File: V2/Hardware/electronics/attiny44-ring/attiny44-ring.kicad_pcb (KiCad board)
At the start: 2 copper layers, 35 x 70 mm, 20 parts, among them J1 CHAIN_IN, J2 CHAIN_OUT, J3 28BYJ-48, J4 HOME_SENSOR, J5 AVR_ISP_2X3, J6 5V_INJECT, U1 ATtiny44A-SS, U2 ULN2003A

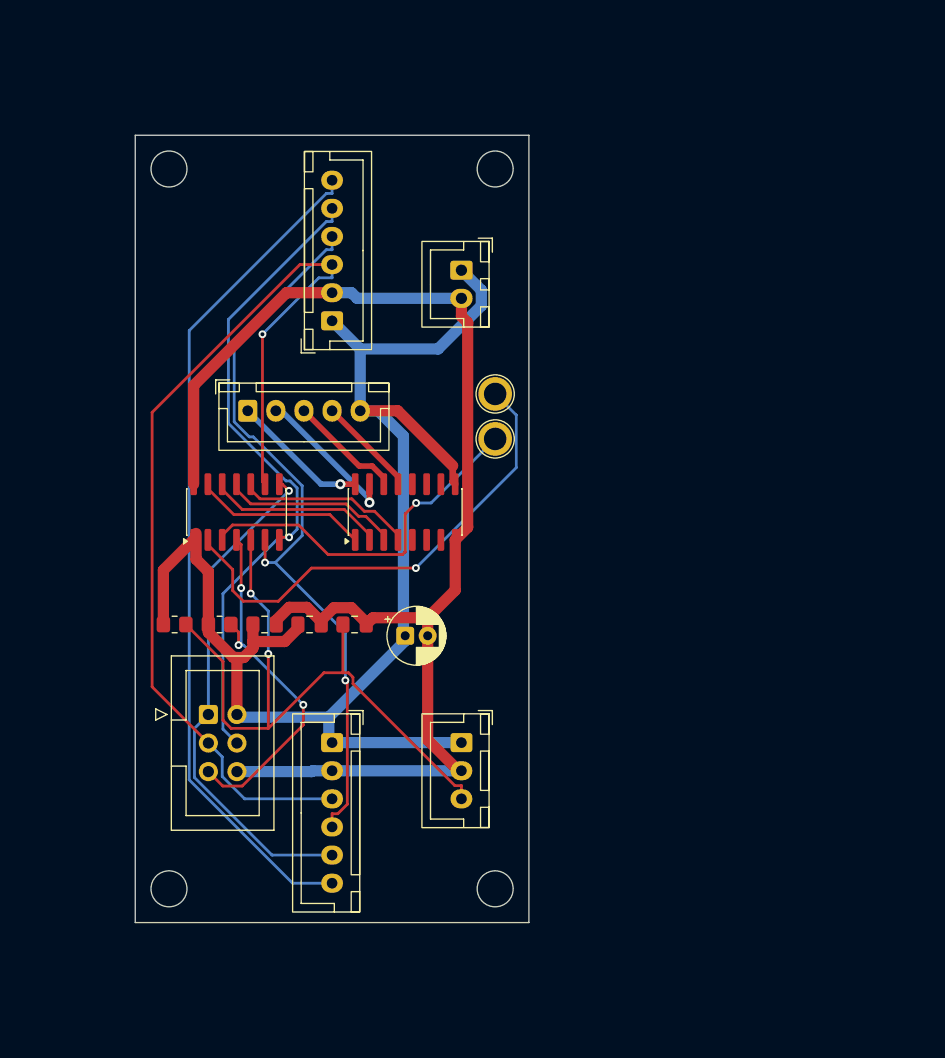
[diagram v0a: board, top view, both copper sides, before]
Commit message: Redesign ATtiny44 ring board for milling
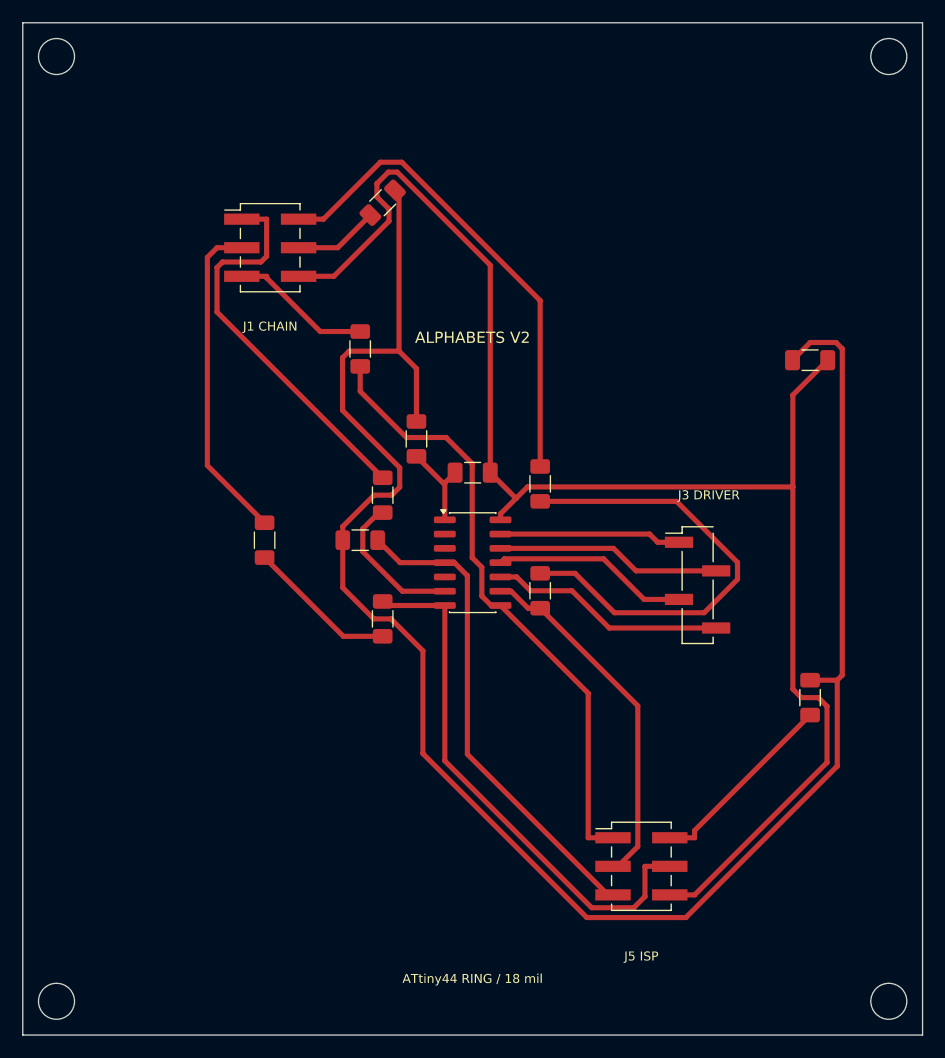
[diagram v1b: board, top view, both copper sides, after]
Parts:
- removed C3: 10n HOME filter, Capacitor_SMD:C_0805_2012Metric_Pad1.18x1.45mm_HandSolder
- removed C4: 47u 10V, Capacitor_THT:CP_Radial_D5.0mm_P2.00mm
- removed J2: CHAIN_OUT, Connector_JST:JST_XH_B6B-XH-A_1x06_P2.50mm_Vertical
- removed J4: HOME_SENSOR, Connector_JST:JST_XH_B3B-XH-A_1x03_P2.50mm_Vertical
- removed J6: 5V_INJECT, Connector_JST:JST_XH_B2B-XH-A_1x02_P2.50mm_Vertical
- removed R1: 10k HOME pull-up, Resistor_SMD:R_0805_2012Metric_Pad1.20x1.40mm_HandSolder
- removed TP1: PB0, TestPoint:TestPoint_Plated_Hole_D2.0mm
- removed TP2: PB1, TestPoint:TestPoint_Plated_Hole_D2.0mm
- removed U2: ULN2003A, Package_SO:SOIC-16_3.9x9.9mm_P1.27mm
- added JP16: 0R CLOCK MCU bridge 1206, Resistor_SMD:R_1206_3216Metric_Pad1.30x1.75mm_HandSolder, F.Cu at (136.0, 140.5)
- added JP17: 0R DATA chain bridge 1206, Resistor_SMD:R_1206_3216Metric_Pad1.30x1.75mm_HandSolder, F.Cu at (111.5, 136.0)
- added JP18: 0R MCU power bridge 1206, Resistor_SMD:R_1206_3216Metric_Pad1.30x1.75mm_HandSolder, F.Cu at (125.0, 127.0)
- added JP19: 0R CHAIN power bridge 1206, Resistor_SMD:R_1206_3216Metric_Pad1.30x1.75mm_HandSolder, F.Cu at (122.0, 106.0)
- added JP20: 0R ISP VCC bridge 1206, Resistor_SMD:R_1206_3216Metric_Pad1.30x1.75mm_HandSolder, F.Cu at (160.0, 150.0)
- added JP5: 0R CLOCK input jumper 1206, Resistor_SMD:R_1206_3216Metric_Pad1.30x1.75mm_HandSolder, F.Cu at (136.0, 131.0)
- added JP6: 0R LATCH input jumper 1206, Resistor_SMD:R_1206_3216Metric_Pad1.30x1.75mm_HandSolder, F.Cu at (122.0, 132.0)
- added JP7: 0R DATA input jumper 1206, Resistor_SMD:R_1206_3216Metric_Pad1.30x1.75mm_HandSolder, F.Cu at (122.0, 143.0)
- added JP8: 0R CHAIN DATA_OUT jumper 1206, Resistor_SMD:R_1206_3216Metric_Pad1.30x1.75mm_HandSolder, F.Cu at (120.0, 119.0)
- C1: value 100n MCU -> 100n MCU 1206; footprint Capacitor_SMD:C_0805_2012Metric_Pad1.18x1.45mm_HandSolder -> Capacitor_SMD:C_1206_3216Metric_Pad1.33x1.80mm_HandSolder
- C2: value 100n DRIVER -> 10u BULK 1206; footprint Capacitor_SMD:C_0805_2012Metric_Pad1.18x1.45mm_HandSolder -> Capacitor_SMD:C_1206_3216Metric_Pad1.33x1.80mm_HandSolder
- J1: value CHAIN_IN -> CHAIN_RING; footprint Connector_JST:JST_XH_B6B-XH-A_1x06_P2.50mm_Vertical -> Connector_PinHeader_2.54mm:PinHeader_2x03_P2.54mm_Vertical_SMD
- J3: value 28BYJ-48 -> STEPPER_DRIVER_IN; footprint Connector_JST:JST_XH_B5B-XH-A_1x05_P2.50mm_Vertical -> Connector_PinHeader_2.54mm:PinHeader_1x04_P2.54mm_Vertical_SMD_Pin1Left
- J5: footprint Connector_IDC:IDC-Header_2x03_P2.54mm_Vertical -> Connector_PinHeader_2.54mm:PinHeader_2x03_P2.54mm_Vertical_SMD
- R2: value 10k RESET pull-up -> 10k RESET pull-up 1206; footprint Resistor_SMD:R_0805_2012Metric_Pad1.20x1.40mm_HandSolder -> Resistor_SMD:R_1206_3216Metric_Pad1.30x1.75mm_HandSolder
- moved C2 50.3 mm to (160.0, 120.0)
- moved J3 42.9 mm to (150.0, 140.0)
- moved J5 40.8 mm to (145.0, 165.0)
- moved H2 36.4 mm to (167.0, 93.0)
- moved H4 36.4 mm to (167.0, 177.0)
- moved C1 22.9 mm to (130.0, 130.0)
- moved U1 21.5 mm to (130.0, 138.0), turned to 0 degrees
- moved R2 14.6 mm to (120.0, 136.0)
- moved H1 14.1 mm to (93.0, 93.0)
- moved H3 14.1 mm to (93.0, 177.0)
- moved J1 8.51 mm to (112.0, 110.0), turned to 0 degrees
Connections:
- net DATA_OUT renamed DATA_OUT_A
- C1 pad 1: +5V -> +5V_U1
- J1 pad 1: +5V -> LATCH_TOP
- J1 pad 2: GND -> CLOCK_TOP
- J1 pad 3: CLOCK -> DATA_CHAIN_IN
- J1 pad 4: LATCH -> +5V_CHAIN
- J1 pad 5: DATA_IN -> DATA_OUT_CHAIN
- J1 pad 6: RETURN -> GND
- J3 pad 1: COIL_A -> MOTOR1
- J3 pad 2: COIL_B -> MOTOR2
- J3 pad 3: COIL_C -> MOTOR3
- J3 pad 4: COIL_D -> MOTOR4
- J5 pad 2: +5V -> ISP_VCC
- J5 pad 3: CLOCK -> CLOCK_U1
- U1 pad 1: +5V -> +5V_U1
- U1 pad 2: PB0 -> unconnected-(U1-PB0-Pad2)
- U1 pad 3: PB1 -> unconnected-(U1-PB1-Pad3)
- U1 pad 5: HOME -> unconnected-(U1-HOME/PB2-Pad5)
- U1 pad 6: LATCH -> LATCH_A
- U1 pad 9: CLOCK -> CLOCK_U1
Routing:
- net CLOCK: track 89.9 -> 0.00 mm, vias 1 -> 0
- net RETURN: track 75.4 -> 0.00 mm
- net LATCH: track 66.6 -> 0.00 mm, vias 2 -> 0
- net HOME: track 60.8 -> 0.00 mm, vias 2 -> 0
- net CLOCK_TOP: track 0.00 -> 43.4 mm
- net PB0: track 43.3 -> 0.00 mm, vias 1 -> 0
- net CLOCK_A: track 0.00 -> 41.5 mm
- net +5V: track 127.9 -> 164.2 mm
- net LATCH_TOP: track 0.00 -> 35.1 mm
- net PB1: track 32.4 -> 0.00 mm, vias 1 -> 0
- net CLOCK_U1: track 0.00 -> 31.9 mm
- net DATA_CHAIN_IN: track 0.00 -> 29.1 mm
- net ISP_VCC: track 0.00 -> 17.4 mm
- net GND: track 117.9 -> 135.0 mm
- net COIL_B: track 13.5 -> 0.00 mm, vias 1 -> 0
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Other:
- board size 35 x 70 mm -> 80 x 90 mm
- board text added: "ALPHABETS V2"
- board text added: "ATtiny44 RING / 18 mil"
- board text added: "J1 CHAIN"
- board text added: "J3 DRIVER"
- board text removed: "4 LATCH 5 DATA 6 RETURN"
- board text removed: "ALPHABETS V2 / ATtiny44 SPI RING"
- board text removed: "J1 RING IN"
- board text removed: "J2 RING OUT"
- board text removed: "J3 MOTOR A B C D +5"
- board text removed: "J4 HOME"
- board text removed: "J6 5V"
- board text removed: "R1 R2 C1 C2 C3 C4"
- board text removed: "RING: 1 +5V 2 GND 3 CLOCK"
- board text removed: "U1 ATtiny44"
- board text removed: "U2 ULN2003"

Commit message: Compact ATtiny44 ring PCB to 50x57 mm
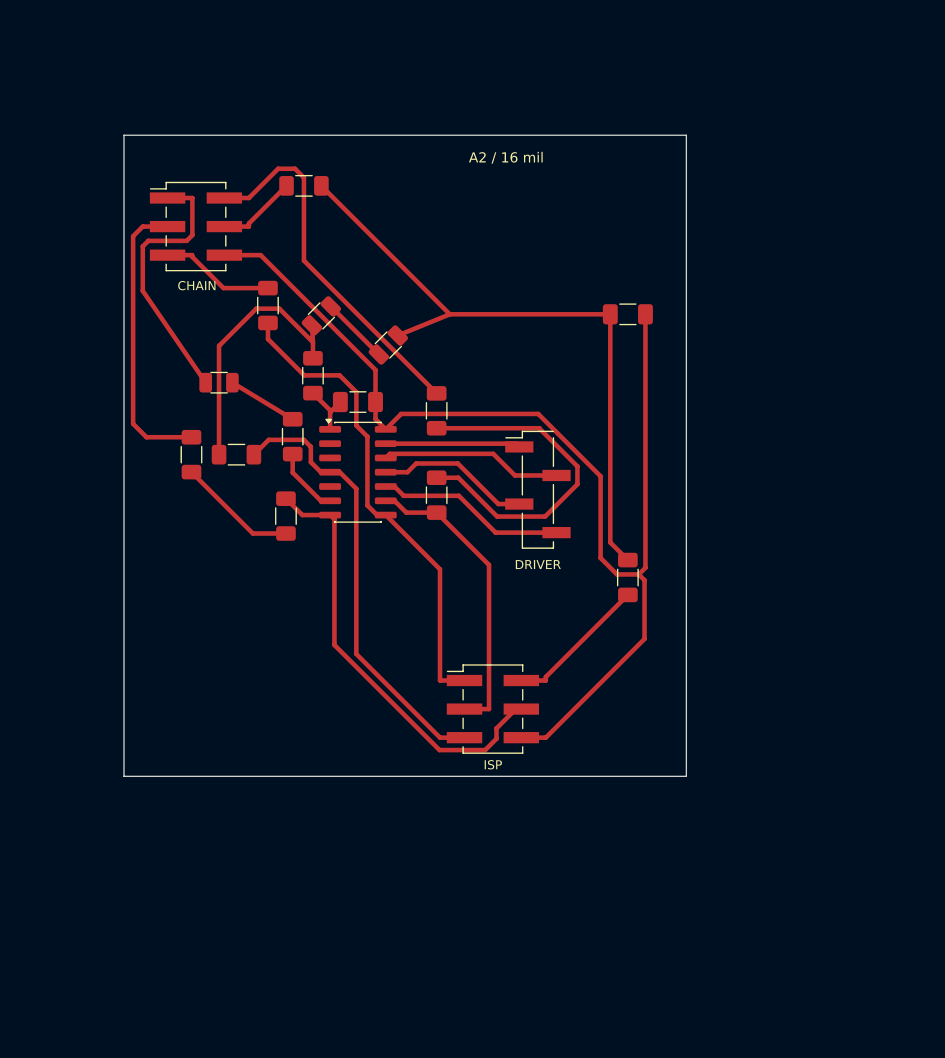
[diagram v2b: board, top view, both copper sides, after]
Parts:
- removed H1, H2, H3, H4: M3, MountingHole:MountingHole_3.2mm_M3
- added JP21: 0R POWER crossover 1 1206, Alphabets:R_1206_3216Metric_CompactCrossover, F.Cu at (122.5, 118.7)
- added JP22: 0R LATCH crossover 1206, Alphabets:R_1206_3216Metric_CompactCrossover, F.Cu at (107.5, 122.0)
- added JP23: 0R POWER crossover 2 1206, Alphabets:R_1206_3216Metric_CompactCrossover, F.Cu at (116.5, 116.1)
- moved JP20 19.4 mm to (143.8, 139.3)
- moved J5 19.2 mm to (131.8, 151.0)
- moved C2 16.7 mm to (143.8, 115.9)
- moved J3 16.5 mm to (135.8, 131.5)
- moved R2 13.4 mm to (109.0, 128.4)
- moved U1 13.0 mm to (119.8, 130.0)
- moved JP7 12.5 mm to (113.4, 133.9)
- moved JP16 12.5 mm to (126.8, 132.0)
- moved C1 12.0 mm to (119.8, 123.7)
- moved JP5 11.3 mm to (126.8, 124.5)
- moved JP18 10.8 mm to (115.8, 121.4)
- moved JP17 10.0 mm to (105.0, 128.4)
- moved JP6 9.54 mm to (114.0, 126.8)
- moved JP8 9.06 mm to (111.8, 115.1)
- moved JP19 7.16 mm to (115.0, 104.5), turned to 0 degrees
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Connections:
- C2 pad 1: +5V -> +5V_TOP
- J1 pad 1: LATCH_TOP -> LATCH_CONN
- JP19 pad 2: +5V -> +5V_TOP
- JP20 pad 2: +5V -> +5V_TOP
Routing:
- net +5V: track 164.2 -> 23.6 mm
- net +5V_TOP: track 0.00 -> 57.9 mm
- net GND: track 135.0 -> 100.5 mm
- net LATCH_TOP: track 35.1 -> 6.27 mm
- net LATCH_CONN: track 0.00 -> 24.2 mm
- net DATA_OUT_A: track 55.1 -> 42.6 mm
- net CLOCK_A: track 41.5 -> 30.6 mm
- net CLOCK_TOP: track 43.4 -> 32.5 mm
- net DATA_IN: track 48.0 -> 38.8 mm
- net LATCH_A: track 13.1 -> 6.01 mm
- net +5V_MID: track 0.00 -> 6.04 mm
- net CLOCK_U1: track 31.9 -> 26.5 mm
- net ISP_VCC: track 17.4 -> 12.8 mm
- net MOTOR1: track 16.2 -> 12.0 mm
- net MOTOR4: track 21.1 -> 16.9 mm
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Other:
- board size 80 x 90 mm -> 50 x 57 mm
- board text added: "A2 / 16 mil"
- board text added: "CHAIN"
- board text added: "DRIVER"
- board text added: "ISP"
- board text removed: "ALPHABETS V2"
- board text removed: "ATtiny44 RING / 18 mil"
- board text removed: "J1 CHAIN"
- board text removed: "J3 DRIVER"
- board text removed: "J5 ISP"

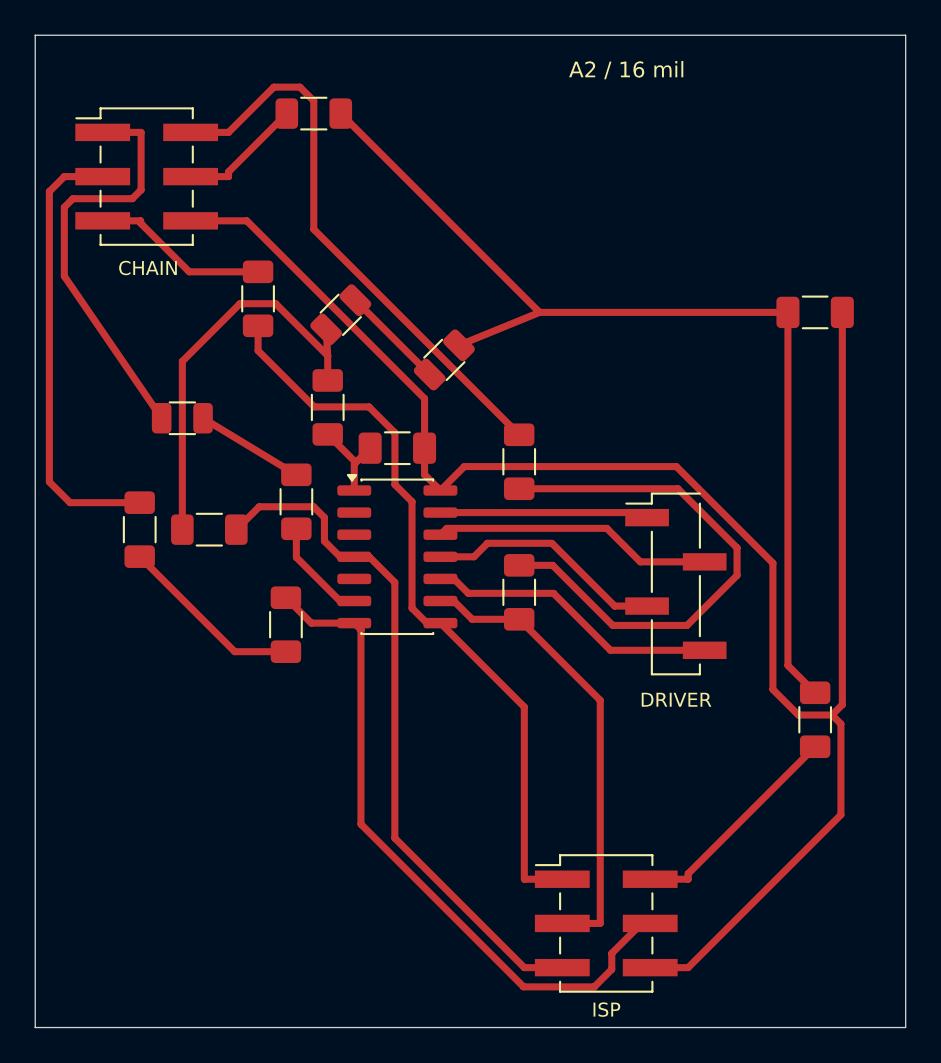
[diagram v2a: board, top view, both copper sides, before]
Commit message: Place ISP beside ATtiny44 on compact board
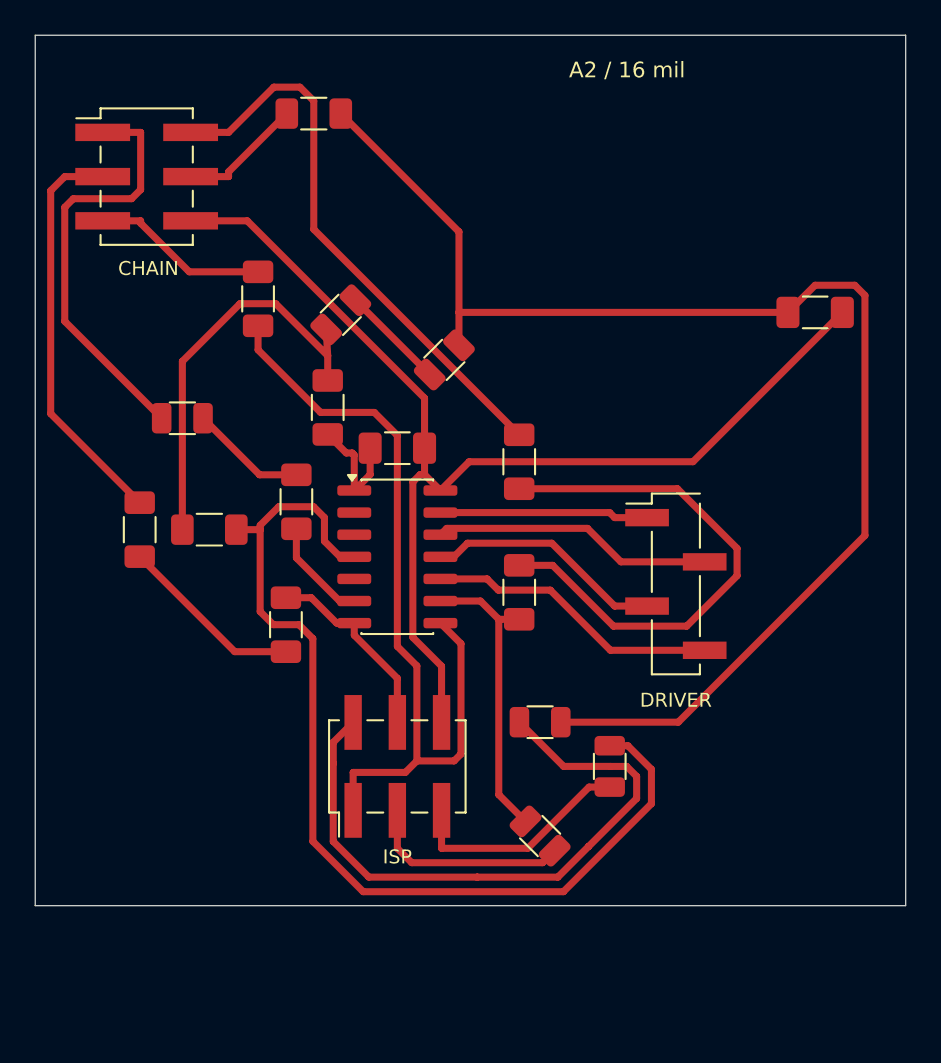
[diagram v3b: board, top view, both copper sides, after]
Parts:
- added JP24: 0R ISP RESET crossover 1206, Alphabets:R_1206_3216Metric_CompactCrossover, F.Cu at (132.0, 142.0)
- added JP25: 0R ISP SCK crossover 1206, Alphabets:R_1206_3216Metric_CompactCrossover, F.Cu at (128.0, 146.0)
- JP20: footprint Resistor_SMD:R_1206_3216Metric_Pad1.30x1.75mm_HandSolder -> Alphabets:R_1206_3216Metric_CompactCrossover
- moved JP20 15.8 mm to (128.0, 139.5), turned to 0 degrees
- moved J5 15.0 mm to (119.8, 142.0), turned to 90 degrees
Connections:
- J5 pad 3: CLOCK_U1 -> CLOCK_ISP
- J5 pad 5: RESET -> RESET_ISP
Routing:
- net GND: track 100.5 -> 66.0 mm
- net DATA_IN: track 38.8 -> 11.3 mm
- net ISP_VCC: track 12.8 -> 36.8 mm
- net +5V_TOP: track 57.9 -> 76.0 mm
- net RESET: track 39.6 -> 57.1 mm
- net RESET_ISP: track 0.00 -> 13.3 mm
- net CLOCK_ISP: track 0.00 -> 11.8 mm
- net CLOCK_U1: track 26.5 -> 17.2 mm
- net DATA_OUT_A: track 42.6 -> 47.4 mm
- net DATA_CHAIN_IN: track 25.8 -> 23.4 mm
- net +5V_U1: track 5.09 -> 6.86 mm
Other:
- board size 50 x 57 mm -> 50 x 50 mm

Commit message: Add organic wide-track ATtiny44 board finish
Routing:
- added copper zone on F.Cu, net +5V
- added copper zone on F.Cu, net +5V_CHAIN
- added copper zone on F.Cu, net +5V_MID
- added copper zone on F.Cu, net +5V_TOP
- added copper zone on F.Cu, net +5V_U1
- added copper zone on F.Cu, net CLOCK_A
- added copper zone on F.Cu, net CLOCK_ISP
- added copper zone on F.Cu, net CLOCK_TOP
- added copper zone on F.Cu, net CLOCK_U1
- added copper zone on F.Cu, net DATA_CHAIN_IN
- added copper zone on F.Cu, net DATA_IN
- added copper zone on F.Cu, net DATA_OUT_A
- added copper zone on F.Cu, net DATA_OUT_CHAIN
- added copper zone on F.Cu, net DATA_TOP
- added copper zone on F.Cu, net GND
- added copper zone on F.Cu, net ISP_VCC
- added copper zone on F.Cu, net LATCH_A
- added copper zone on F.Cu, net LATCH_CONN
- added copper zone on F.Cu, net LATCH_TOP
- added copper zone on F.Cu, net MOTOR1
- added copper zone on F.Cu, net MOTOR2
- added copper zone on F.Cu, net MOTOR3
- added copper zone on F.Cu, net MOTOR4
- added copper zone on F.Cu, net RESET
- added copper zone on F.Cu, net RESET_ISP
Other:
- board text added: "A2 / 16-20 mil"
- board text removed: "A2 / 16 mil"
